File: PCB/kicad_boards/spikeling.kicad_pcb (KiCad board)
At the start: 2 copper layers, 55.1 x 65.2 mm, 21 parts, among them J1 D_IN1, J2 D_IN2, J3 A_IN, J4 D_OUT, J5 A_OUT, J6 Vin, J7 Arduino1-15, J8 Arduino16-30, SW1 Button

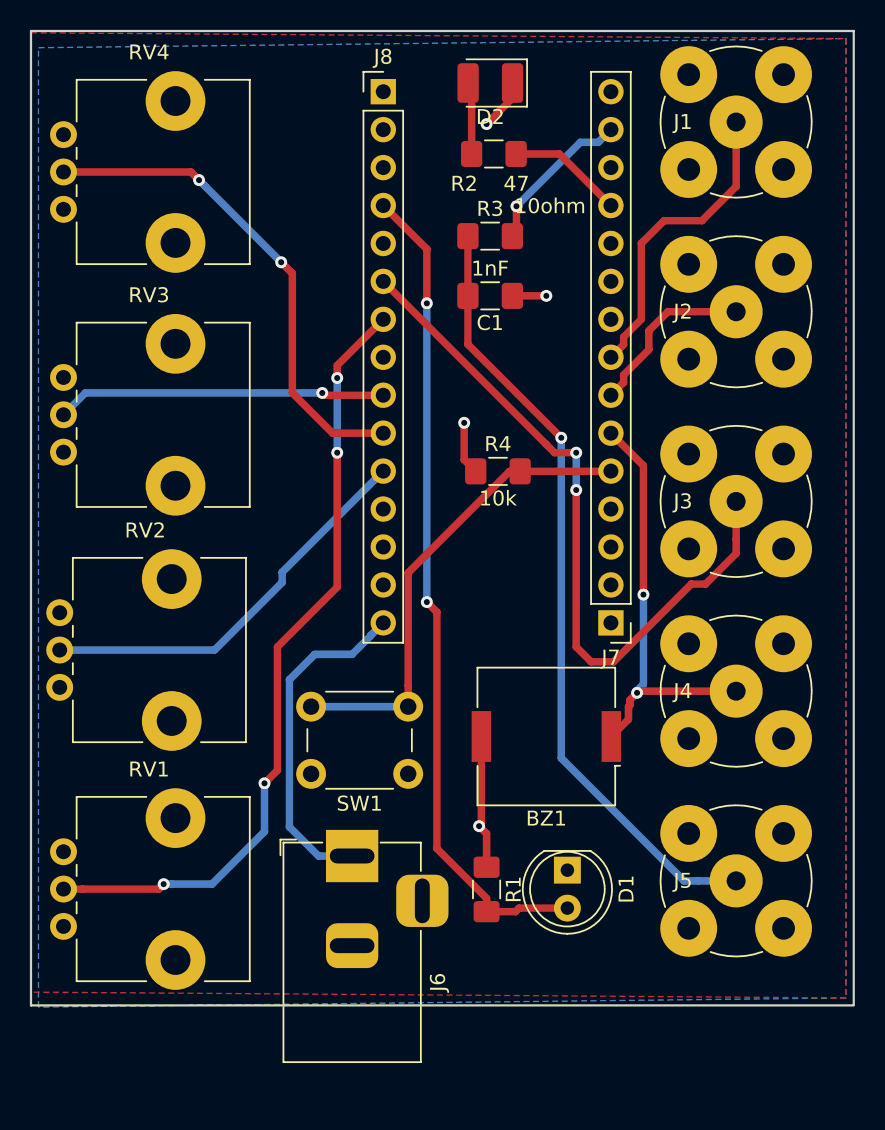
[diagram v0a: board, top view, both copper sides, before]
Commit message: update smd version of board
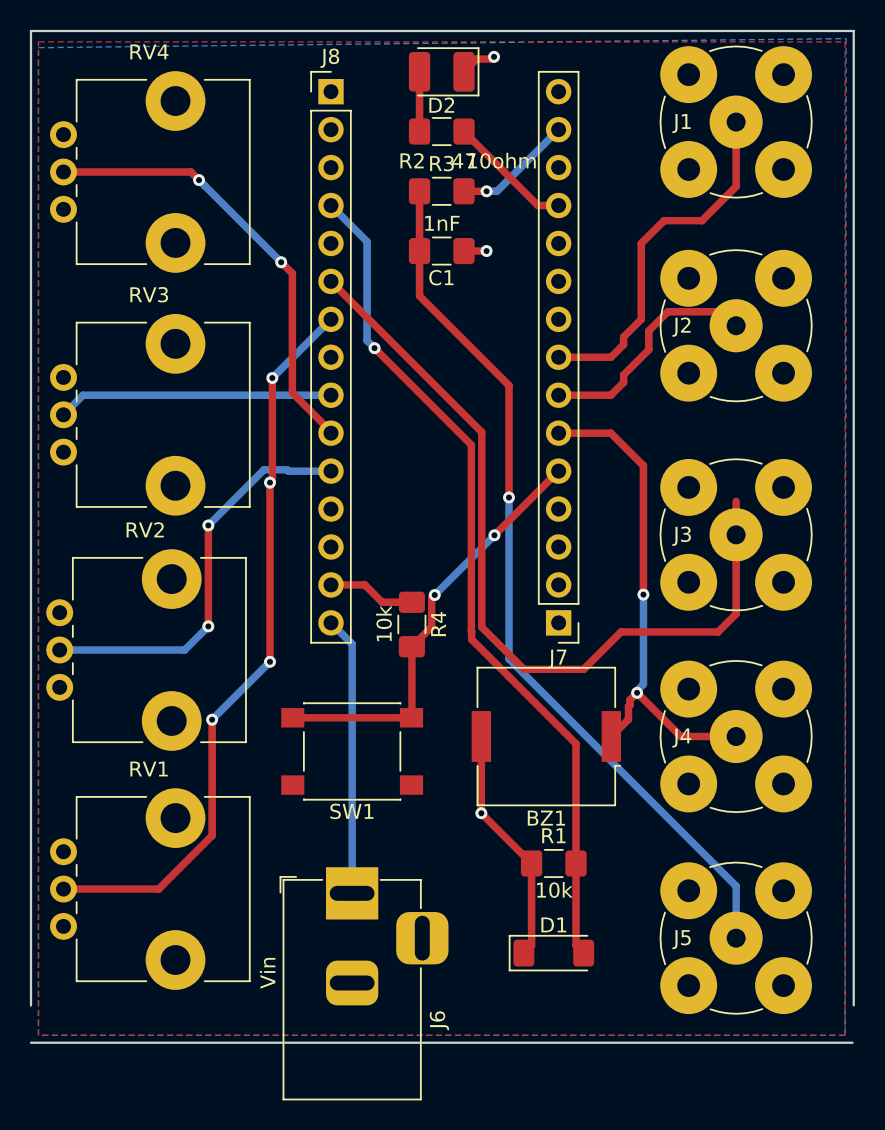
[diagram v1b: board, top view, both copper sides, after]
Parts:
- D1: footprint LED_THT:LED_D5.0mm_Clear -> LED_SMD:LED_1806_4516Metric
- SW1: footprint Button_Switch_THT:SW_PUSH_6mm_H5mm -> Button_Switch_SMD:SW_Push_1P1T_NO_6x6mm_H9.5mm
- moved R4 11.8 mm to (166.0, 88.5), turned to 270 degrees
- moved D1 5.63 mm to (175.5, 110.5), turned to 0 degrees
- moved R1 4.82 mm to (175.5, 104.5), turned to 0 degrees
- moved C1 4.41 mm to (168.0, 63.5)
- moved R3 4.41 mm to (168.0, 59.5)
- moved SW1 4.04 mm to (162.0, 97.0)
- moved J5 3.84 mm to (187.7, 109.5)
- moved R2 3.80 mm to (168.0, 55.5)
- moved J7 3.50 mm to (175.8, 88.4)
- moved J8 3.50 mm to (160.6, 52.8)
- moved D2 3.34 mm to (168.0, 51.5)
- moved J4 3.04 mm to (187.7, 96.0)
- moved J6 2.50 mm to (162.0, 106.5)
- moved J3 2.24 mm to (187.7, 82.5)
- moved J2 0.94 mm to (187.7, 68.5)
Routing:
- net GND: track 18.3 -> 25.9 mm, vias 4 -> 3
- net A_in: track 48.3 -> 55.8 mm, vias 2 -> 0
- net Net-(C1-Pad2): track 52.6 -> 58.8 mm
- net D_out: track 28.8 -> 33.4 mm
- net Vin: track 22.7 -> 18.7 mm
- net RV3: track 22.1 -> 18.5 mm, vias 1 -> 0
- net D_in2: track 11.7 -> 15.2 mm
- net D_in1: track 20.7 -> 24.2 mm
- net RV4: track 33.3 -> 29.9 mm
- net RV1: track 52.6 -> 49.3 mm
- net push_button: track 31.9 -> 28.5 mm, vias 0 -> 2
- net A_out: track 10.6 -> 8.05 mm
- net photodiode: track 55.6 -> 57.1 mm, vias 2 -> 1
- net Net-(D2-Pad2): track 4.85 -> 4.00 mm
- net (no net): track 0.64 -> 0.00 mm
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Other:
- board size 55.1 x 65.2 mm -> 55.1 x 67.7 mm
